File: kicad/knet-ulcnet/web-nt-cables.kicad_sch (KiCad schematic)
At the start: 9 parts, among them P1 EXT, P2 NET

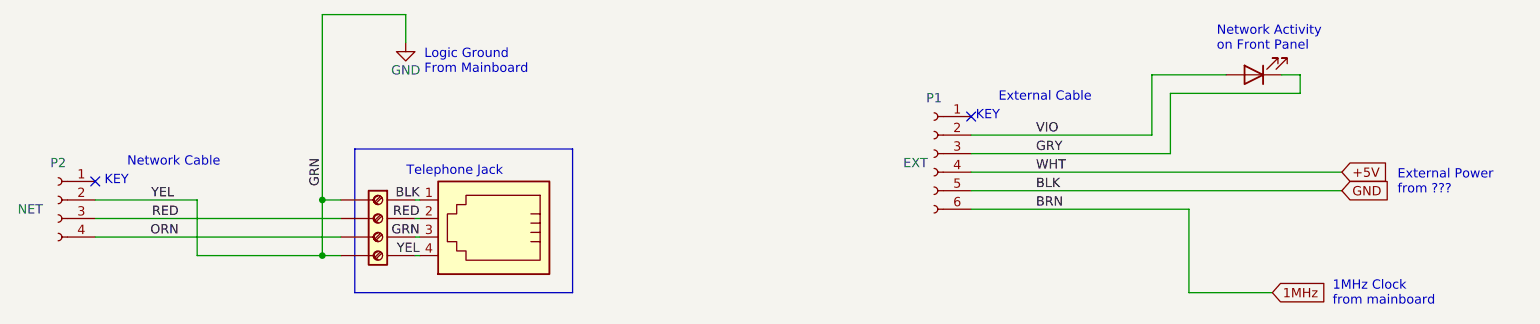
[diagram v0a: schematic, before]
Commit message: get web-nt schematic to pass ERC
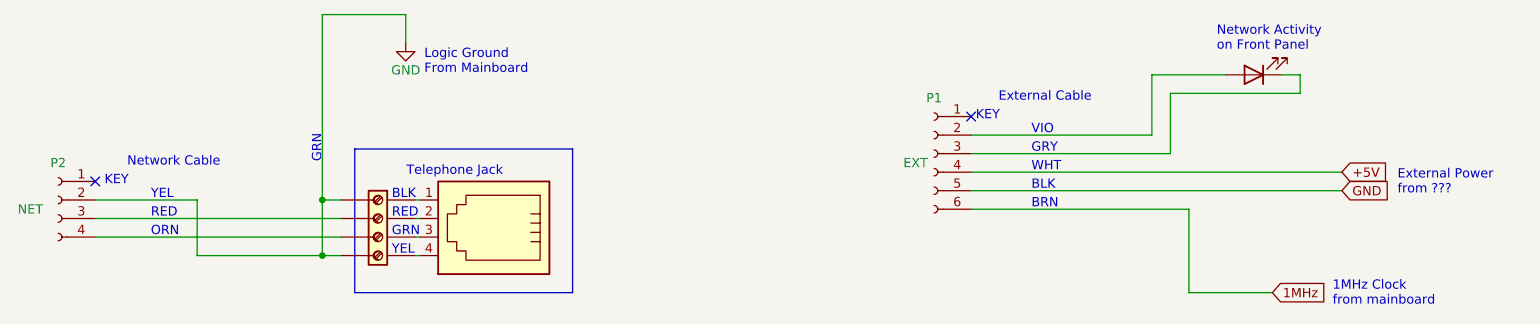
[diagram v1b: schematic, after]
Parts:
- removed J? (x4): Conn_01x01_Female, symbol Connector:Conn_01x01_Female
- added JX3: Conn_01x04_Female, symbol Connector:Conn_01x04_Female
- gave numbers to parts that had none: 3
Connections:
- net GND: now also JX3.1 (Pin_1), JX3.4 (Pin_4); no longer JX1.1, JX1.3, JX1.4, JX2.1 (Pin_1), JX2.3 (Pin_3), JX2.4 (Pin_4)
- net GRY: no longer names the net of D0.1 (K), P1.3 (Pin_3)
- net ORN: no longer names the net of P2.4 (Pin_4)
- net ORN: now also JX3.3 (Pin_3)
- net RED: no longer names the net of JX1.2, JX2.2 (Pin_2)
- net RED: no longer P2.3 (Pin_3)
- net VIO: no longer names the net of D0.2 (A), P1.2 (Pin_2)
- new net: JX1.1, JX2.1 (Pin_1)
- new net: JX1.3, JX2.3 (Pin_3)
- new net: JX1.4, JX2.4 (Pin_4)
- new net: JX3.2 (Pin_2), P2.3 (Pin_3)
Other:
- note added: "BLK"
- note added: "BRN"
- note added: "GRN"
- note added: "GRY"
- note added: "ORN"
- note added: "RED"
- note added: "VIO"
- note added: "WHT"
- note added: "YEL"
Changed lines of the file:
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@@
     (stroke (width 0) (type default) (color 0 0 0 0))
   )
+  (text "GRN" (at 71.12 69.85 0)
+    (effects (font (size 1.27 1.27)) (justify left bottom))
+  )
+  (text "YEL" (at 71.12 72.39 0)
+    (effects (font (size 1.27 1.27)) (justify left bottom))
+  )
+  (text "VIO" (at 158.75 55.88 0)
+    (effects (font (size 1.27 1.27)) (justify left bottom))
+  )
   (text "KEY" (at 151.13 53.975 0)
+    (effects (font (size 1.27 1.27)) (justify left bottom))
+  )
+  (text "GRN" (at 61.595 59.69 90)
     (effects (font (size 1.27 1.27)) (justify left bottom))
   )
@@
     (effects (font (size 1.27 1.27)) (justify left bottom))
   )
+  (text "BLK" (at 158.75 63.5 0)
+    (effects (font (size 1.27 1.27)) (justify left bottom))
+  )
   (text "External Power\nfrom ???" (at 208.915 64.135 0)
     (effects (font (size 1.27 1.27)) (justify left bottom))
   )
+  (text "BRN" (at 158.75 66.04 0)
+    (effects (font (size 1.27 1.27)) (justify left bottom))
+  )
+  (text "YEL" (at 38.1 64.77 0)
+    (effects (font (size 1.27 1.27)) (justify left bottom))
+  )
+  (text "GRY" (at 158.75 58.42 0)
+    (effects (font (size 1.27 1.27)) (justify left bottom))
+  )
   (text "Logic Ground\nFrom Mainboard" (at 75.565 47.625 0)
     (effects (font (size 1.27 1.27)) (justify left bottom))
   )
+  (text "RED" (at 71.12 67.31 0)
+    (effects (font (size 1.27 1.27)) (justify left bottom))
+  )
+  (text "WHT" (at 158.75 60.96 0)
+    (effects (font (size 1.27 1.27)) (justify left bottom))
+  )
+  (text "ORN" (at 38.1 69.85 0)
+    (effects (font (size 1.27 1.27)) (justify left bottom))
+  )
   (text "KEY" (at 31.75 62.865 0)
     (effects (font (size 1.27 1.27)) (justify left bottom))
   )
+  (text "RED" (at 38.1 67.31 0)
+    (effects (font (size 1.27 1.27)) (justify left bottom))
+  )
   (text "Network Activity\non Front Panel" (at 184.15 44.45 0)
+    (effects (font (size 1.27 1.27)) (justify left bottom))
+  )
+  (text "BLK" (at 71.12 64.77 0)
     (effects (font (size 1.27 1.27)) (justify left bottom))
   )
   (text "Telephone Jack" (at 86.36 61.595 180)
     (effects (font (size 1.27 1.27)) (justify right bottom))
-  )
-  (label "YEL" (at 41.275 64.77 180)
-    (effects (font (size 1.27 1.27)) (justify right bottom))
-  )
-  (label "YEL" (at 74.93 72.39 180)
-    (effects (font (size 1.27 1.27)) (justify right bottom))
-  )
-  (label "GRN" (at 61.595 62.865 90)
-    (effects (font (size 1.27 1.27)) (justify left bottom))
-  )
-  (label "WHT" (at 159.385 60.96 0)
-    (effects (font (size 1.27 1.27)) (justify left bottom))
-  )
-  (label "RED" (at 41.91 67.31 180)
-    (effects (font (size 1.27 1.27)) (justify right bottom))
-  )
-  (label "GRN" (at 74.93 69.85 180)
-    (effects (font (size 1.27 1.27)) (justify right bottom))
-  )
-  (label "RED" (at 74.93 67.31 180)
-    (effects (font (size 1.27 1.27)) (justify right bottom))
-  )
-  (label "BLK" (at 74.93 64.77 180)
-    (effects (font (size 1.27 1.27)) (justify right bottom))
-  )
-  (label "BRN" (at 159.385 66.04 0)
-    (effects (font (size 1.27 1.27)) (justify left bottom))
-  )
-  (label "GRY" (at 159.385 58.42 0)
-    (effects (font (size 1.27 1.27)) (justify left bottom))
-  )
-  (label "BLK" (at 159.385 63.5 0)
-    (effects (font (size 1.27 1.27)) (justify left bottom))
-  )
-  (label "ORN" (at 41.91 69.85 180)
-    (effects (font (size 1.27 1.27)) (justify right bottom))
-  )
-  (label "VIO" (at 159.385 55.88 0)
-    (effects (font (size 1.27 1.27)) (justify left bottom))
   )
   (global_label "GND" (shape input) (at 201.295 63.5 0) (fields_autoplaced)
@@
     )
   )
-  (symbol (lib_id "Connector:Conn_01x01_Female") (at 69.215 67.31 0) (mirror x) (unit 1)
-    (in_bom yes) (on_board yes) (fields_autoplaced)
-    (property "Reference" "J?" (id 0) (at 71.12 68.5801 0)
-      (effects (font (size 1.27 1.27)) (justify left) hide)
-    )
-    (property "Value" "Conn_01x01_Female" (id 1) (at 71.12 66.0401 0)
-      (effects (font (size 1.27 1.27)) (justify left) hide)
-    )
-    (property "Footprint" "" (id 2) (at 69.215 67.31 0)
-      (effects (font (size 1.27 1.27)) hide)
-    )
-    (property "Datasheet" "~" (id 3) (at 69.215 67.31 0)
-      (effects (font (size 1.27 1.27)) hide)
-    )
-    (pin "1")
-  )
-  (symbol (lib_id "Connector:Conn_01x01_Female") (at 69.215 69.85 0) (mirror x) (unit 1)
-    (in_bom yes) (on_board yes) (fields_autoplaced)
-    (property "Reference" "J?" (id 0) (at 71.12 71.1201 0)
-      (effects (font (size 1.27 1.27)) (justify left) hide)
-    )
-    (property "Value" "Conn_01x01_Female" (id 1) (at 71.12 68.5801 0)
-      (effects (font (size 1.27 1.27)) (justify left) hide)
-    )
-    (property "Footprint" "" (id 2) (at 69.215 69.85 0)
-      (effects (font (size 1.27 1.27)) hide)
-    )
-    (property "Datasheet" "~" (id 3) (at 69.215 69.85 0)
-      (effects (font (size 1.27 1.27)) hide)
-    )
-    (pin "1")
-  )
   (symbol (lib_id "Connector:Screw_Terminal_01x04") (at 69.215 67.31 0) (mirror y) (unit 1)
     (in_bom yes) (on_board yes) (fields_autoplaced)
-    (property "Reference" "J?" (id 0) (at 69.215 79.375 0)
+    (property "Reference" "JX2" (id 0) (at 69.215 79.375 0)
       (effects (font (size 1.27 1.27)) hide)
     )
@@
     (pin "6")
   )
-  (symbol (lib_id "Connector:Conn_01x01_Female") (at 69.215 72.39 0) (mirror x) (unit 1)
-    (in_bom yes) (on_board yes) (fields_autoplaced)
-    (property "Reference" "J?" (id 0) (at 71.12 73.6601 0)
-      (effects (font (size 1.27 1.27)) (justify left) hide)
-    )
-    (property "Value" "Conn_01x01_Female" (id 1) (at 71.12 71.1201 0)
-      (effects (font (size 1.27 1.27)) (justify left) hide)
-    )
-    (property "Footprint" "" (id 2) (at 69.215 72.39 0)
-      (effects (font (size 1.27 1.27)) hide)
-    )
-    (property "Datasheet" "~" (id 3) (at 69.215 72.39 0)
-      (effects (font (size 1.27 1.27)) hide)
-    )
-    (pin "1")
-  )
-  (symbol (lib_id "Connector:Conn_01x01_Female") (at 69.215 64.77 0) (mirror x) (unit 1)
-    (in_bom yes) (on_board yes) (fields_autoplaced)
-    (property "Reference" "J?" (id 0) (at 71.12 66.0401 0)
-      (effects (font (size 1.27 1.27)) (justify left) hide)
-    )
-    (property "Value" "Conn_01x01_Female" (id 1) (at 71.12 63.5001 0)
-      (effects (font (size 1.27 1.27)) (justify left) hide)
-    )
-    (property "Footprint" "" (id 2) (at 69.215 64.77 0)
-      (effects (font (size 1.27 1.27)) hide)
-    )
-    (property "Datasheet" "~" (id 3) (at 69.215 64.77 0)
-      (effects (font (size 1.27 1.27)) hide)
-    )
-    (pin "1")
-  )
   (symbol (lib_id "Connector:Conn_01x04_Female") (at 25.4 64.77 0) (mirror y) (unit 1)
     (in_bom yes) (on_board yes)
@@
   (symbol (lib_id "Device:LED") (at 189.23 47.625 180) (unit 1)
     (in_bom yes) (on_board yes) (fields_autoplaced)
-    (property "Reference" "D?" (id 0) (at 190.8175 40.005 0)
+    (property "Reference" "D0" (id 0) (at 190.8175 40.005 0)
       (effects (font (size 1.27 1.27)) hide)
     )
@@
   (symbol (lib_id "Connector:RJ9") (at 85.09 67.31 180) (unit 1)
     (in_bom yes) (on_board yes) (fields_autoplaced)
-    (property "Reference" "J?" (id 0) (at 85.09 80.645 0)
+    (property "Reference" "JX1" (id 0) (at 85.09 80.645 0)
       (effects (font (size 1.27 1.27)) hide)
     )
@@
   (symbol (lib_id "power:GND") (at 73.025 43.18 0) (unit 1)
     (in_bom yes) (on_board yes)
-    (property "Reference" "#PWR?" (id 0) (at 73.025 49.53 0)
+    (property "Reference" "#PWR0132" (id 0) (at 73.025 49.53 0)
       (effects (font (size 1.27 1.27)) hide)
     )
@@
     (pin "1")
   )
+  (symbol (lib_name "Conn_01x04_Female_1") (lib_id "Connector:Conn_01x04_Female") (at 69.215 67.31 0) (unit 1)
+    (in_bom yes) (on_board yes) (fields_autoplaced)
+    (property "Reference" "JX3" (id 0) (at 71.12 67.3099 0)
+      (effects (font (size 1.27 1.27)) (justify left) hide)
+    )
+    (property "Value" "Conn_01x04_Female" (id 1) (at 71.12 69.8499 0)
+      (effects (font (size 1.27 1.27)) (justify left) hide)
+    )
+    (property "Footprint" "" (id 2) (at 69.215 67.31 0)
+      (effects (font (size 1.27 1.27)) hide)
+    )
+    (property "Datasheet" "~" (id 3) (at 69.215 67.31 0)
+      (effects (font (size 1.27 1.27)) hide)
+    )
+    (pin "1")
+    (pin "2")
+    (pin "3")
+    (pin "4")
+  )
 )
